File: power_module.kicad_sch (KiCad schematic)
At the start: 16 parts, among them J1 Conn_01x02_Pin, J2 Conn_01x02_Pin, U1 TPS54202DDC

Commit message: MCU migration completed
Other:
- title: (none) -> RBC by UGS
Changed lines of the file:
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@@
 (kicad_sch (version 20230121) (generator eeschema)
   (paper "A4")
+  (title_block
+    (title "RBC by UGS")
+    (date "2023-09-04")
+    (rev "2.0")
+  )
   (junction (at 105.41 62.23) (diameter 0) (color 0 0 0 0)
   )

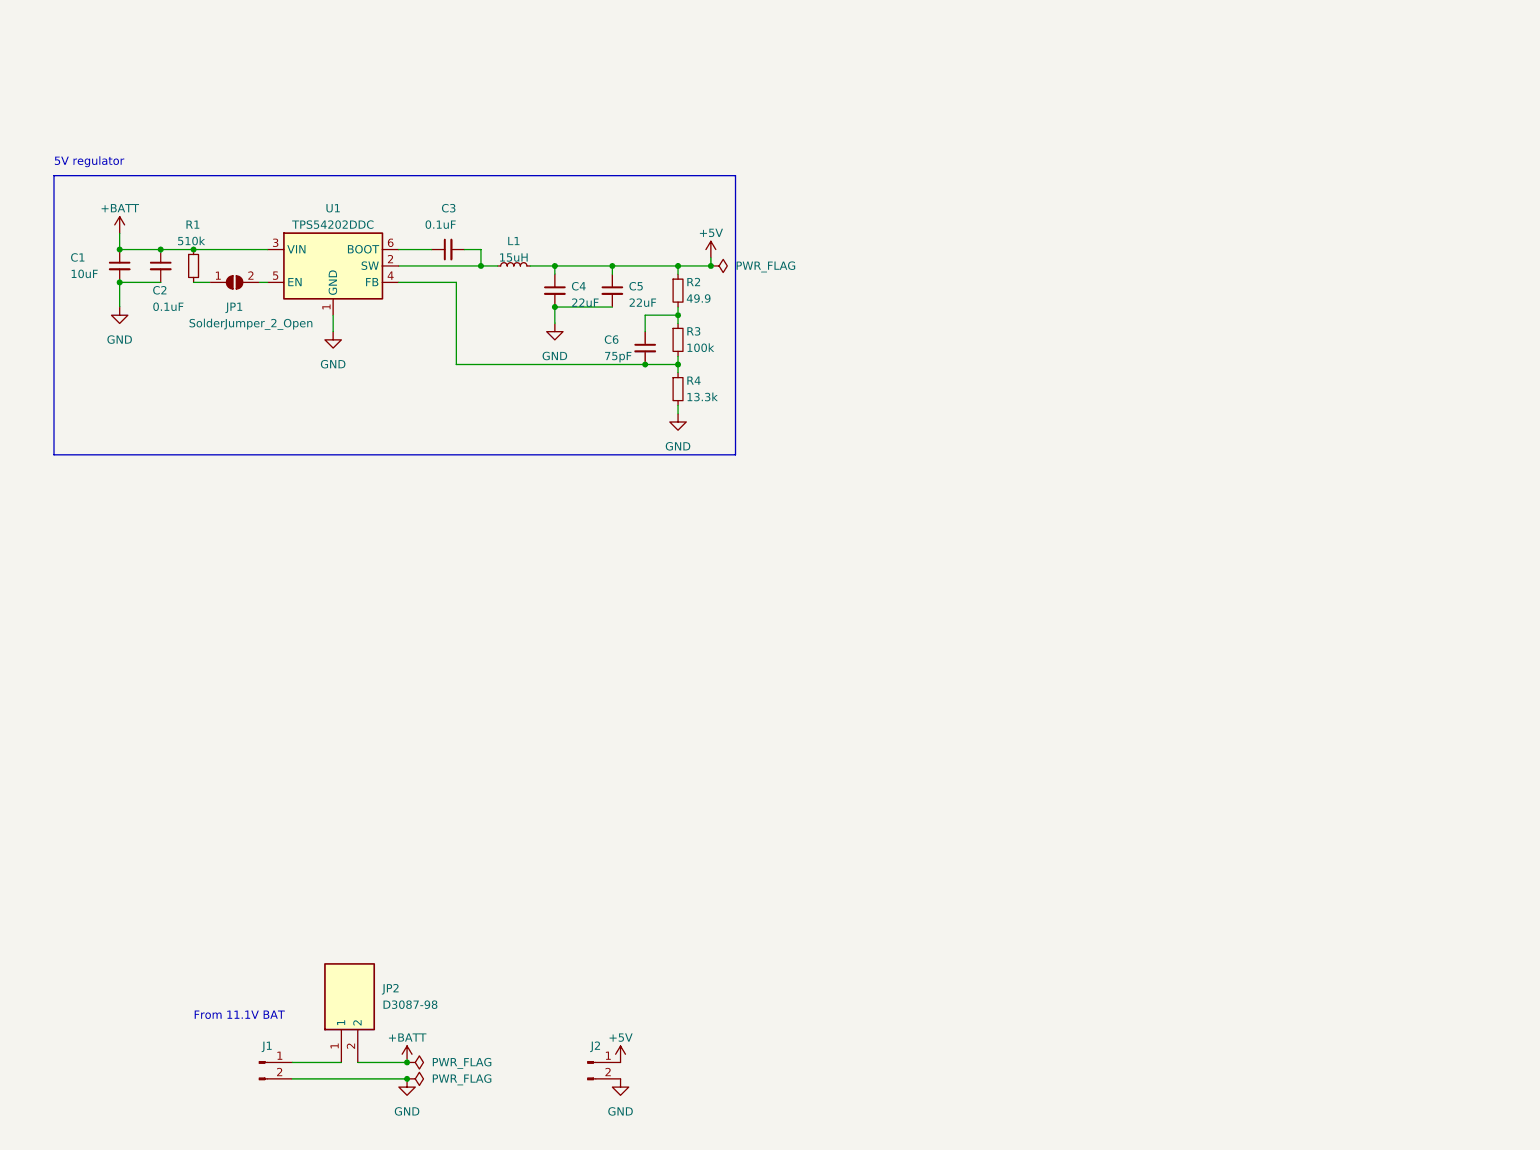
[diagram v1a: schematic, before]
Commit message: 5V regulator WIP
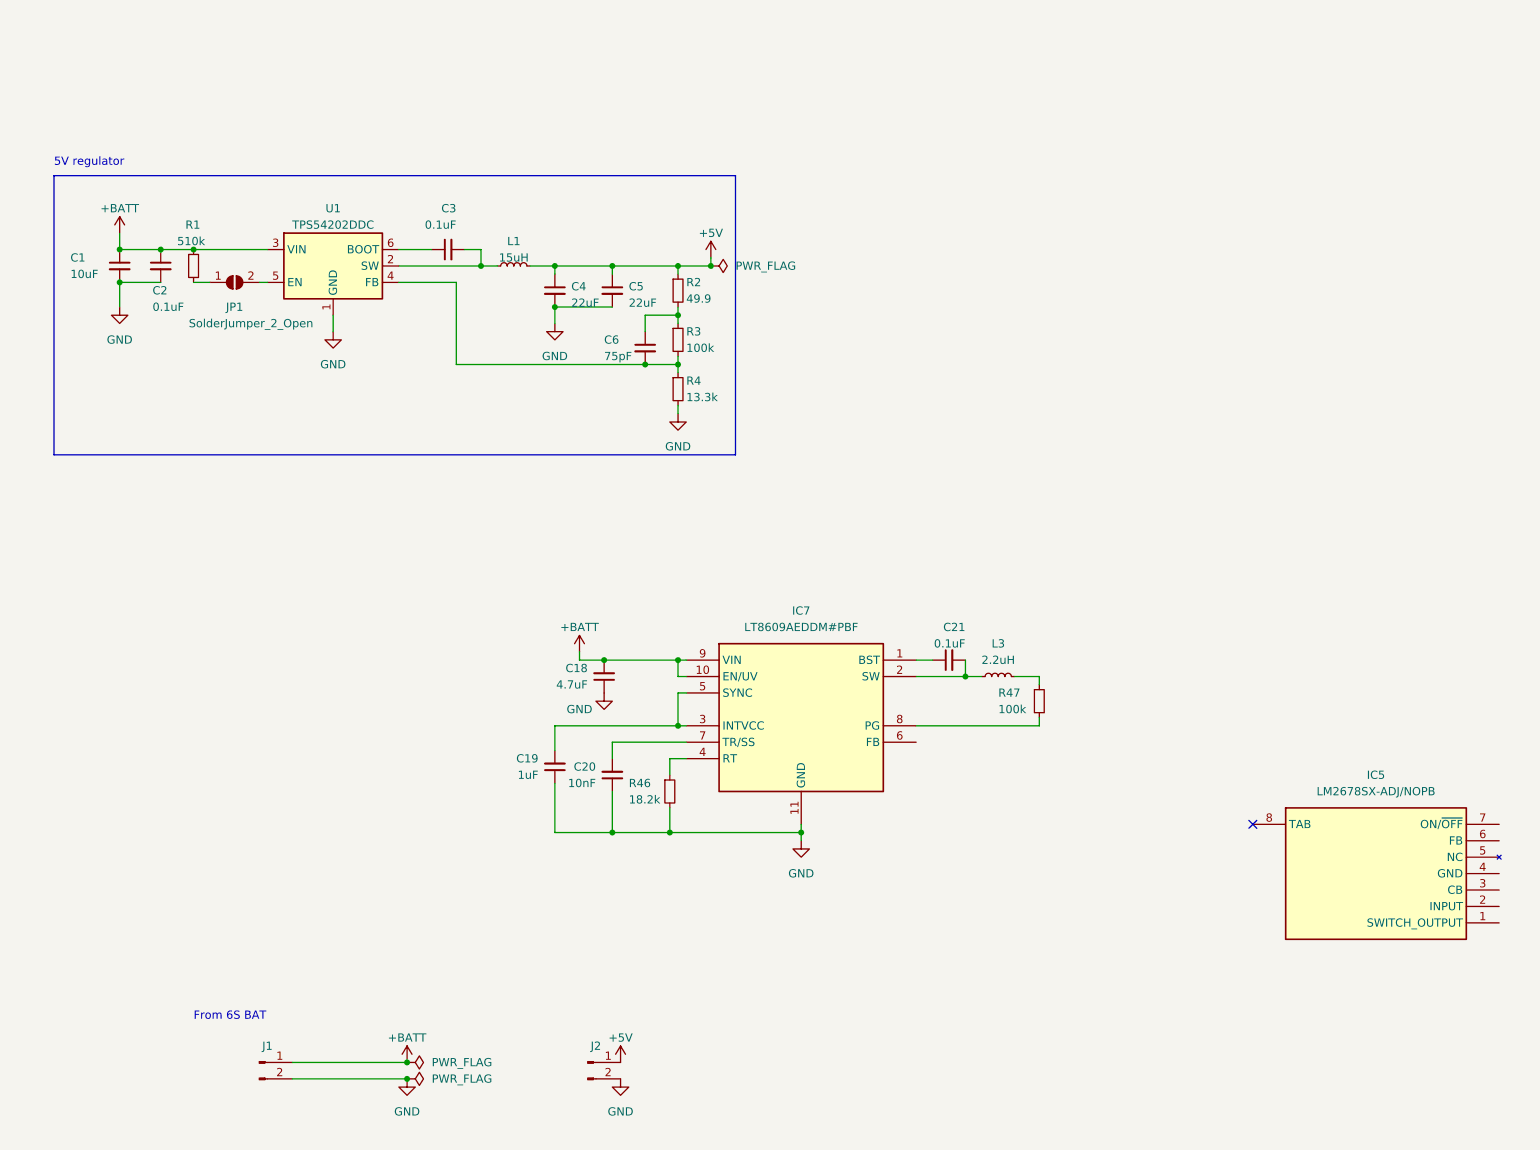
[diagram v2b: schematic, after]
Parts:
- removed JP2: D3087-98, SamacSys_Parts:D308798, symbol SamacSys_Parts:D3087-98
- added C18: 4.7uF, Capacitor_SMD:C_0603_1608Metric_Pad1.08x0.95mm_HandSolder, symbol Device:C_Small
- added C19: 1uF, Capacitor_SMD:C_0603_1608Metric_Pad1.08x0.95mm_HandSolder, symbol Device:C_Small
- added C20: 10nF, Capacitor_SMD:C_0603_1608Metric_Pad1.08x0.95mm_HandSolder, symbol Device:C_Small
- added C21: 0.1uF, Capacitor_SMD:C_0603_1608Metric_Pad1.08x0.95mm_HandSolder, symbol Device:C_Small
- added IC5: LM2678SX-ADJ/NOPB, KTW0007B, symbol SamacSys_Parts:LM2678SX-5.0_NOPB
- added IC7: LT8609AEDDM#PBF, SamacSys_Parts:SON50P300X300X80-11N-D, symbol SamacSys_Parts:LT8609AEDDM#PBF
- added L3: 2.2uH, LQH3NPH150MMEL:IND_LQH3NPH150MMEL, symbol Device:L_Small
- added R46: 18.2k, Resistor_SMD:R_0805_2012Metric_Pad1.20x1.40mm_HandSolder, symbol Device:R_Small
- added R47: 100k, Resistor_SMD:R_0805_2012Metric_Pad1.20x1.40mm_HandSolder, symbol Device:R_Small
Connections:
- net +BATT: now also J1.1 (Pin_1), C18.2, IC7.10 (EN/UV), IC7.9 (VIN)
- net GND: now also C18.1, C19.1, C20.1, IC7.11 (GND), R46.2
- new net: IC7.4 (RT), R46.1
- new net: C21.1, IC7.1 (BST)
- new net: C21.2, IC7.2 (SW), L3.1
- new net: L3.2, R47.1
- new net: IC7.8 (PG), R47.2
- new net: C19.2, IC7.3 (INTVCC), IC7.5 (SYNC)
- new net: C20.2, IC7.7 (TR/SS)
- no-connect marks 0 -> 1
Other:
- note added: "From 6S BAT"
- note removed: "From 11.1V BAT"

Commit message: completed 5V regulator
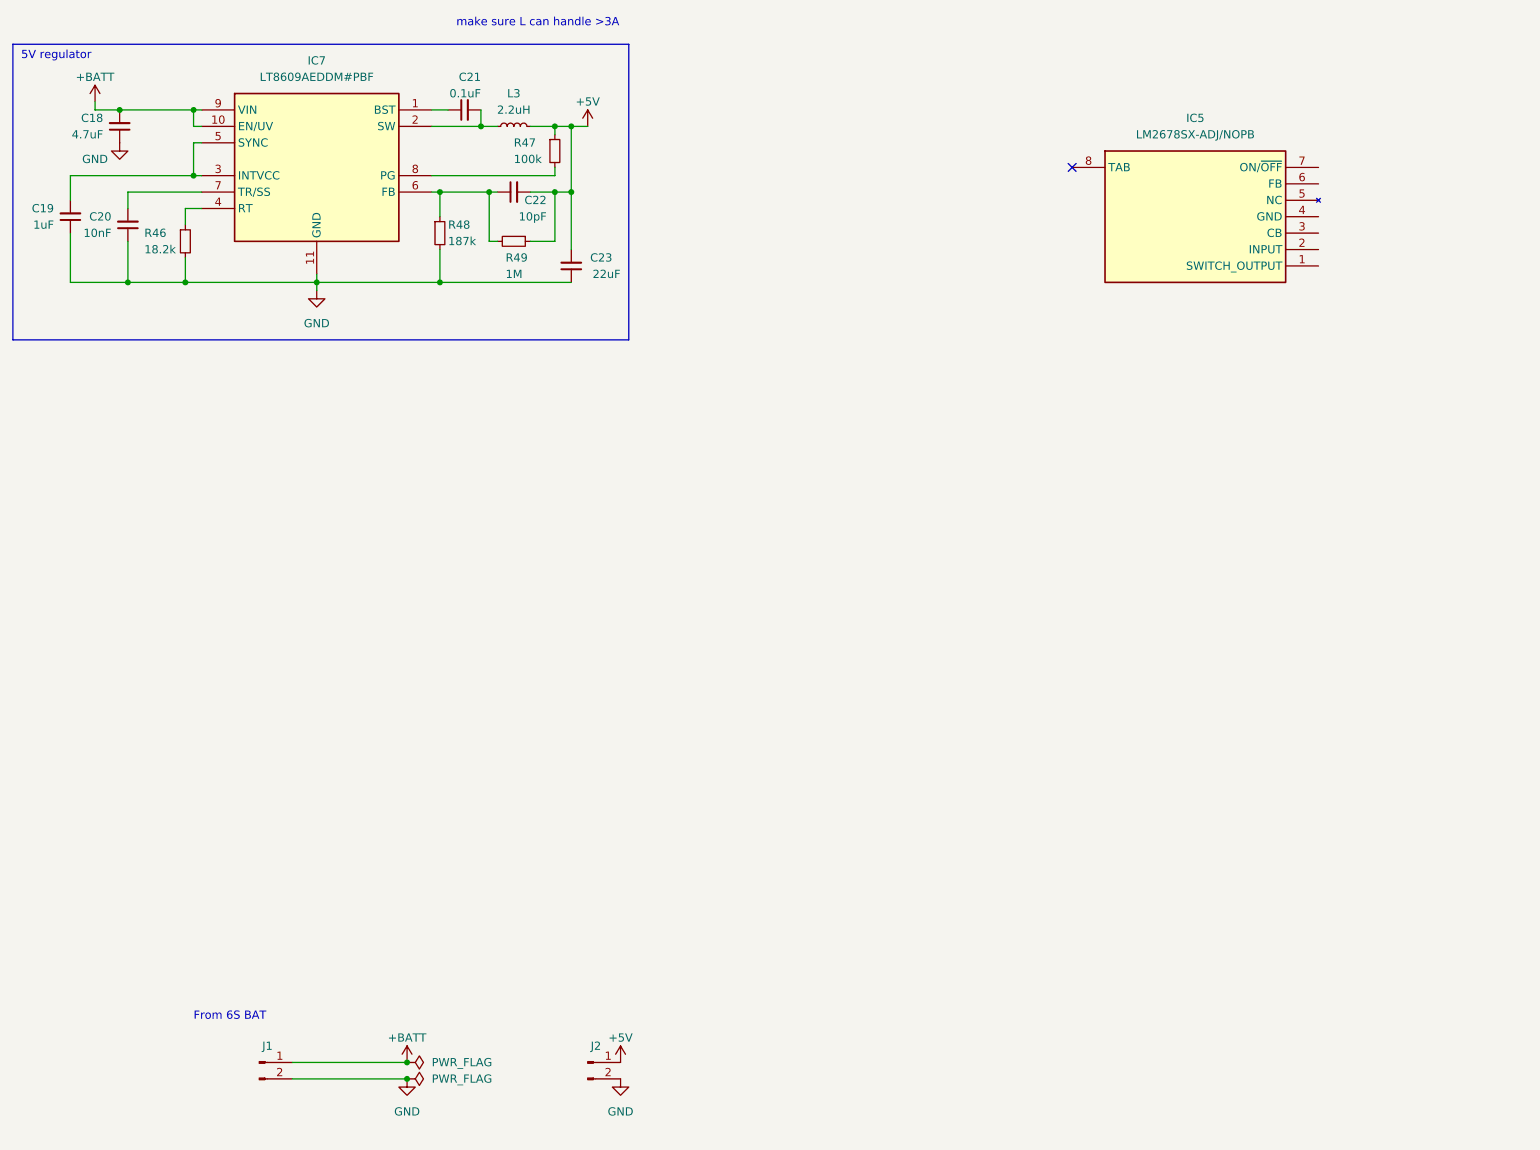
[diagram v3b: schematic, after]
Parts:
- removed C1: 10uF, Capacitor_SMD:C_1206_3216Metric_Pad1.33x1.80mm_HandSolder, symbol Device:C_Small
- removed C2, C3: 0.1uF, Capacitor_SMD:C_0603_1608Metric_Pad1.08x0.95mm_HandSolder, symbol Device:C_Small
- removed C4, C5: 22uF, Capacitor_SMD:C_1206_3216Metric_Pad1.33x1.80mm_HandSolder, symbol Device:C_Small
- removed C6: 75pF, Capacitor_SMD:C_0805_2012Metric_Pad1.18x1.45mm_HandSolder, symbol Device:C_Small
- removed JP1: SolderJumper_2_Open, Jumper:SolderJumper-2_P1.3mm_Open_RoundedPad1.0x1.5mm, symbol Jumper:SolderJumper_2_Open
- removed L1: 15uH, LQH3NPH150MMEL:IND_LQH3NPH150MMEL, symbol Device:L_Small
- removed R1: 510k, Resistor_SMD:R_0805_2012Metric_Pad1.20x1.40mm_HandSolder, symbol Device:R_Small
- removed R2: 49.9, Resistor_SMD:R_0805_2012Metric_Pad1.20x1.40mm_HandSolder, symbol Device:R_Small
- removed R3: 100k, Resistor_SMD:R_1206_3216Metric_Pad1.30x1.75mm_HandSolder, symbol Device:R_Small
- removed R4: 13.3k, Resistor_SMD:R_0805_2012Metric_Pad1.20x1.40mm_HandSolder, symbol Device:R_Small
- removed U1: TPS54202DDC, Package_TO_SOT_SMD:SOT-23-6, symbol Regulator_Switching:TPS54202DDC
- added C22: 10pF, Capacitor_SMD:C_0603_1608Metric_Pad1.08x0.95mm_HandSolder, symbol Device:C_Small
- added C23: 22uF, Capacitor_SMD:C_0603_1608Metric_Pad1.08x0.95mm_HandSolder, symbol Device:C_Small
- added R48: 187k, Resistor_SMD:R_0805_2012Metric_Pad1.20x1.40mm_HandSolder, symbol Device:R_Small
- added R49: 1M, Resistor_SMD:R_0805_2012Metric_Pad1.20x1.40mm_HandSolder, symbol Device:R_Small
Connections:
- net +5V: now also L3.2, R47.1, C22.2, C23.2, R49.1
- net GND: now also C23.1, R48.2
- net at IC7.6 (FB): now also C22.1, R48.1, R49.2
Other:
- note added: "make sure L can handle >3A"
- moved on the sheet: C18, C19, C20, C21, IC5, IC7, L3, R46, R47

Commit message: completed 12V regulators
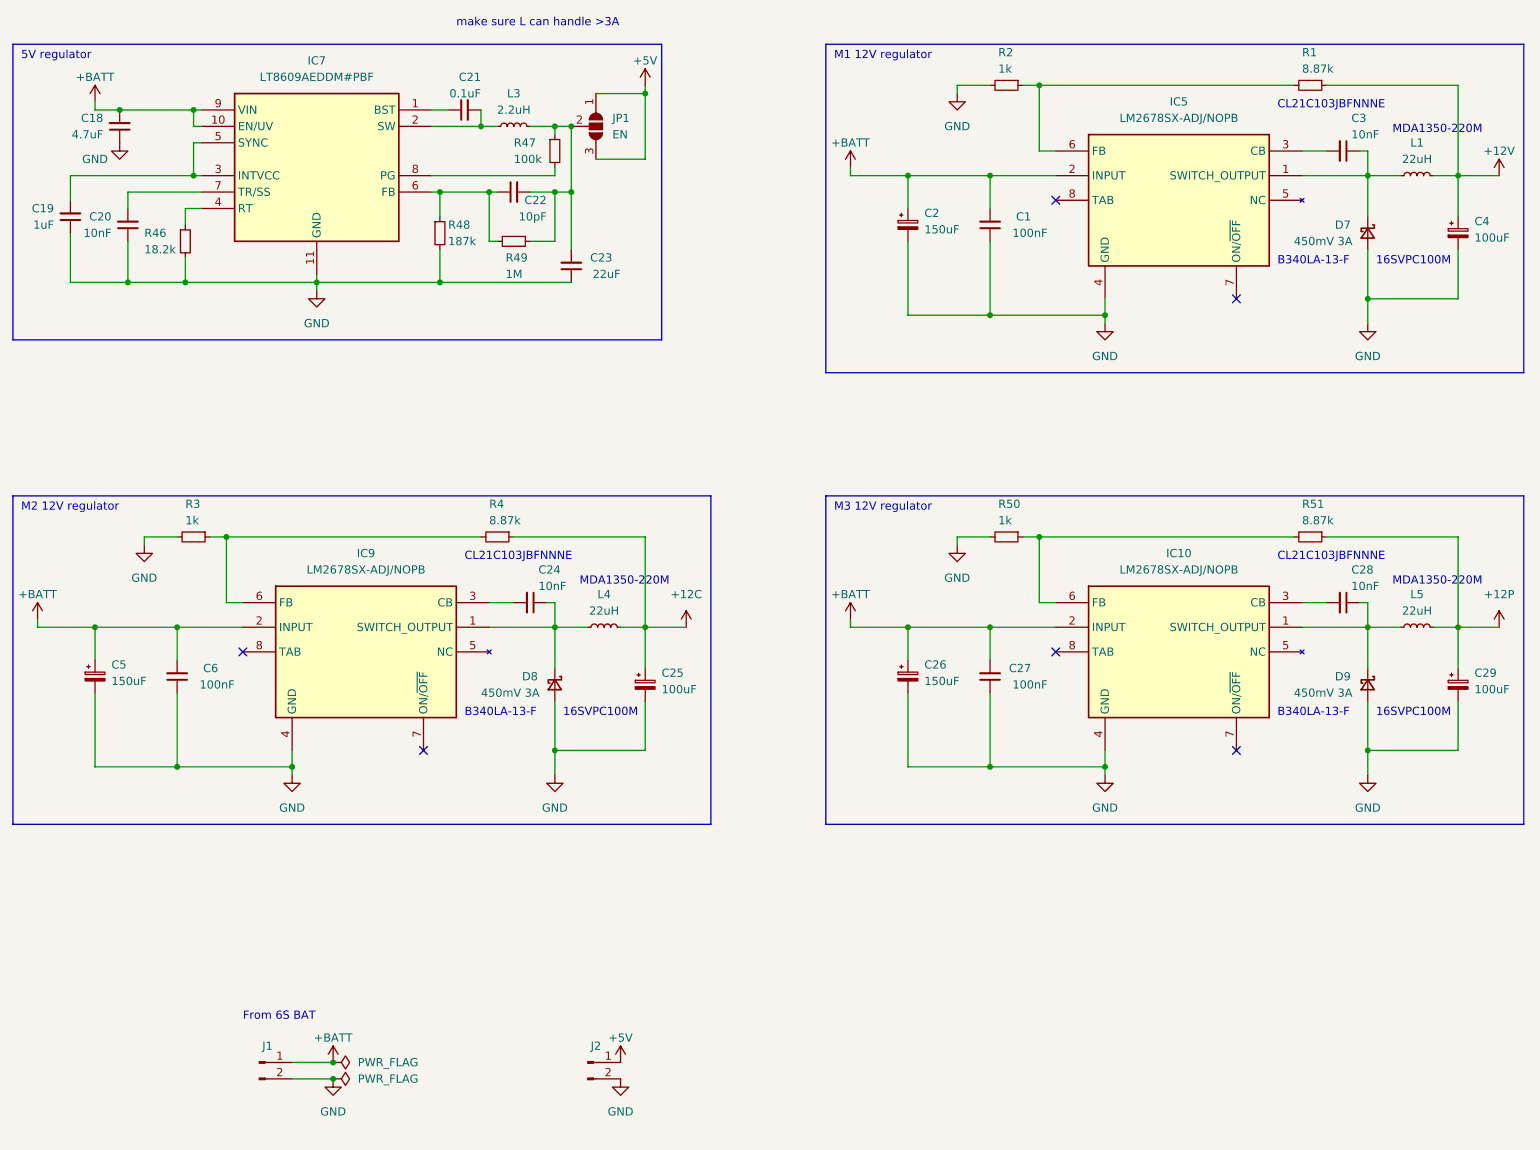
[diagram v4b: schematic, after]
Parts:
- added C1, C27, C6: 100nF, Capacitor_SMD:C_0603_1608Metric_Pad1.08x0.95mm_HandSolder, symbol Device:C_Small
- added C2, C26, C5: 150uF, symbol Device:C_Polarized_Small
- added C24, C28, C3: 10nF, Capacitor_SMD:C_0603_1608Metric_Pad1.08x0.95mm_HandSolder, symbol Device:C_Small
- added C25, C29, C4: 100uF, symbol Device:C_Polarized_Small
- added D7, D8, D9: 450mV 3A, symbol Device:D_Schottky_Small
- added IC10, IC9: LM2678SX-ADJ/NOPB, SamacSys_Parts:KTW0007B, symbol SamacSys_Parts:LM2678SX-5.0_NOPB
- added JP1: EN, Jumper:SolderJumper-3_P2.0mm_Open_TrianglePad1.0x1.5mm, symbol Jumper:SolderJumper_3_Open
- added L1, L4, L5: 22uH, LQH3NPH150MMEL:IND_LQH3NPH150MMEL, symbol Device:L_Small
- added R1, R4, R51: 8.87k, Resistor_SMD:R_0805_2012Metric_Pad1.20x1.40mm_HandSolder, symbol Device:R_Small
- added R2, R3, R50: 1k, Resistor_SMD:R_0805_2012Metric_Pad1.20x1.40mm_HandSolder, symbol Device:R_Small
- IC5: footprint KTW0007B -> SamacSys_Parts:KTW0007B
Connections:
- net +5V: now also JP1.1 (A), JP1.3 (B); no longer C22.2, C23.2, L3.2, R47.1, R49.1
- net +BATT: now also IC5.2 (INPUT), C1.2, C2.1, C26.1, C27.2, C5.1, C6.2, IC10.2 (INPUT), IC9.2 (INPUT)
- net GND: now also IC5.4 (GND), C1.1, C2.2, C25.2, C26.2, C27.1, C29.2, C4.2, C5.2, C6.1, D7.2 (A), D8.2 (A), D9.2 (A), IC10.4 (GND), IC9.4 (GND), R2.2, R3.2, R50.2
- net at IC5.1 (SWITCH_OUTPUT): now also C3.1, D7.1 (K), L1.1
- net at IC5.3 (CB): now also C3.2
- net at IC5.6 (FB): now also R1.2, R2.1
- new net: C28.1, D9.1 (K), IC10.1 (SWITCH_OUTPUT), L5.1
- new net: C28.2, IC10.3 (CB)
- new net: IC10.6 (FB), R50.1, R51.2
- new net: IC9.6 (FB), R3.1, R4.2
- new net: C22.2, C23.2, JP1.2 (C), L3.2, R47.1, R49.1
- new net: C24.1, D8.1 (K), IC9.1 (SWITCH_OUTPUT), L4.1
- new net: C24.2, IC9.3 (CB)
- new net +12C: C25.1, L4.2, R4.1
- new net +12P: C29.1, L5.2, R51.1
- new net +12V: C4.1, L1.2, R1.1
- no-connect marks 1 -> 6
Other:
- note added: "16SVPC100M"
- note added: "B340LA-13-F"
- note added: "CL21C103JBFNNNE"
- note added: "M1 12V regulator"
- note added: "M2 12V regulator"
- note added: "M3 12V regulator"
- note added: "MDA1350-220M"
- moved on the sheet: IC5
